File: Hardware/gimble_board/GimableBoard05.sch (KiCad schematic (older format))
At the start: 38 parts, among them Q1 Q_NMOS_GDS, Q2 Q_NMOS_GDS, Q3 Q_NMOS_GDS, Q4 Q_NMOS_GDS, Q5 Q_NMOS_GDS, Q6 Q_NMOS_GDS, Q7 Q_NMOS_GDS, Q8 Q_NMOS_GDS

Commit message: Fixed MOSFET's
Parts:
- removed D20, D21, D22, D23, D24, D25, D26: LED, symbol Device:LED
- removed Q2, Q3, Q4, Q5, Q6, Q7, Q8: Q_NMOS_GDS, symbol Device:Q_NMOS_GDS
- removed R26, R27, R28, R29, R30, R31, R32: 330, symbol Device:R
- removed R34, R35, R36, R37, R38, R39, R40: 500, symbol Device:R
- added D? (x7): LED, symbol Device:LED
- added Q? (x7): Q_NMOS_GDS, symbol Device:Q_NMOS_GDS
- added R? (x7): 330, symbol Device:R
- added R? (x7): 500, symbol Device:R
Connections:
- net +3V3: now also R25.1, R?.1, R?.1, R?.1, R?.1, R?.1, R?.1, R?.1; no longer R25.2
- net GND: now also Q1.3 (S), Q?.3 (S), Q?.3 (S), Q?.3 (S), Q?.3 (S), Q?.3 (S), Q?.3 (S), Q?.3 (S); no longer Q1.2 (D)
- net Servo_1_PWM: now also R33.1, R?.1, R?.1, R?.1, R?.1, R?.1, R?.1, R?.1; no longer R33.2
- net at D19.2 (A): now also R25.2; no longer R25.1
- net at D19.1 (K): now also Q1.2 (D); no longer Q1.3 (S)
- net at Q1.1 (G): now also R33.2; no longer R33.1
- new net: D?.2 (A), R?.2 (x7)
- new net: D?.1 (K), Q?.2 (D) (x7)
- new net: Q?.1 (G), R?.2 (x7)
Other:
- moved on the sheet: D19, Q1, R25, R33

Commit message: Annotated Symbols
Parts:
- gave numbers to parts that had none: 28
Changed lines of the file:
@@
 Servo_1_PWM
 $Comp
-L Device:R R?
+L Device:R R34
 U 1 1 5F8988CD
 P 3750 2100
-F 0 "R?" V 3650 2100 50  0000 C CNN
+F 0 "R34" V 3650 2100 50  0000 C CNN
 F 1 "330" V 3750 2100 50  0000 C CNN
 F 2 "" V 3680 2100 50  0001 C CNN
@@
 $EndComp
 $Comp
-L Device:LED D?
+L Device:LED D20
 U 1 1 5F8988D3
 P 3300 2100
-F 0 "D?" H 3300 2000 50  0000 C CNN
+F 0 "D20" H 3300 2000 50  0000 C CNN
 F 1 "LED" H 3300 2200 50  0000 C CNN
 F 2 "" H 3300 2100 50  0001 C CNN
@@
 $EndComp
 $Comp
-L Device:Q_NMOS_GDS Q?
+L Device:Q_NMOS_GDS Q2
 U 1 1 5F8988D9
 P 2800 2000
-F 0 "Q?" V 2800 2150 50  0000 C CNN
+F 0 "Q2" V 2800 2150 50  0000 C CNN
 F 1 "Q_NMOS_GDS" V 3050 2050 50  0000 C CNN
 F 2 "" H 3000 2100 50  0001 C CNN
@@
 $EndComp
 $Comp
-L Device:R R?
+L Device:R R26
 U 1 1 5F8988DF
 P 3100 1800
-F 0 "R?" V 3000 1800 50  0000 C CNN
+F 0 "R26" V 3000 1800 50  0000 C CNN
 F 1 "500" V 3100 1800 50  0000 C CNN
 F 2 "" V 3030 1800 50  0001 C CNN
@@
 Servo_1_PWM
 $Comp
-L Device:R R?
+L Device:R R35
 U 1 1 5F8A6B43
 P 3750 2750
-F 0 "R?" V 3650 2750 50  0000 C CNN
+F 0 "R35" V 3650 2750 50  0000 C CNN
 F 1 "330" V 3750 2750 50  0000 C CNN
 F 2 "" V 3680 2750 50  0001 C CNN
@@
 $EndComp
 $Comp
-L Device:LED D?
+L Device:LED D21
 U 1 1 5F8A6B49
 P 3300 2750
-F 0 "D?" H 3300 2650 50  0000 C CNN
+F 0 "D21" H 3300 2650 50  0000 C CNN
 F 1 "LED" H 3300 2850 50  0000 C CNN
 F 2 "" H 3300 2750 50  0001 C CNN
@@
 $EndComp
 $Comp
-L Device:Q_NMOS_GDS Q?
+L Device:Q_NMOS_GDS Q3
 U 1 1 5F8A6B4F
 P 2800 2650
-F 0 "Q?" V 2800 2800 50  0000 C CNN
+F 0 "Q3" V 2800 2800 50  0000 C CNN
 F 1 "Q_NMOS_GDS" V 3050 2700 50  0000 C CNN
 F 2 "" H 3000 2750 50  0001 C CNN
@@
 $EndComp
 $Comp
-L Device:R R?
+L Device:R R27
 U 1 1 5F8A6B55
 P 3100 2450
-F 0 "R?" V 3000 2450 50  0000 C CNN
+F 0 "R27" V 3000 2450 50  0000 C CNN
 F 1 "500" V 3100 2450 50  0000 C CNN
 F 2 "" V 3030 2450 50  0001 C CNN
@@
 Servo_1_PWM
 $Comp
-L Device:R R?
+L Device:R R36
 U 1 1 5F8A6B62
 P 3750 3400
-F 0 "R?" V 3650 3400 50  0000 C CNN
+F 0 "R36" V 3650 3400 50  0000 C CNN
 F 1 "330" V 3750 3400 50  0000 C CNN
 F 2 "" V 3680 3400 50  0001 C CNN
@@
 $EndComp
 $Comp
-L Device:LED D?
+L Device:LED D22
 U 1 1 5F8A6B68
 P 3300 3400
-F 0 "D?" H 3300 3300 50  0000 C CNN
+F 0 "D22" H 3300 3300 50  0000 C CNN
 F 1 "LED" H 3300 3500 50  0000 C CNN
 F 2 "" H 3300 3400 50  0001 C CNN
@@
 $EndComp
 $Comp
-L Device:Q_NMOS_GDS Q?
+L Device:Q_NMOS_GDS Q4
 U 1 1 5F8A6B6E
 P 2800 3300
-F 0 "Q?" V 2800 3450 50  0000 C CNN
+F 0 "Q4" V 2800 3450 50  0000 C CNN
 F 1 "Q_NMOS_GDS" V 3050 3350 50  0000 C CNN
 F 2 "" H 3000 3400 50  0001 C CNN
@@
 $EndComp
 $Comp
-L Device:R R?
+L Device:R R28
 U 1 1 5F8A6B74
 P 3100 3100
-F 0 "R?" V 3000 3100 50  0000 C CNN
+F 0 "R28" V 3000 3100 50  0000 C CNN
 F 1 "500" V 3100 3100 50  0000 C CNN
 F 2 "" V 3030 3100 50  0001 C CNN
@@
 Servo_1_PWM
 $Comp
-L Device:R R?
+L Device:R R37
 U 1 1 5F8C6A5B
 P 3750 4050
-F 0 "R?" V 3650 4050 50  0000 C CNN
+F 0 "R37" V 3650 4050 50  0000 C CNN
 F 1 "330" V 3750 4050 50  0000 C CNN
 F 2 "" V 3680 4050 50  0001 C CNN
@@
 $EndComp
 $Comp
-L Device:LED D?
+L Device:LED D23
 U 1 1 5F8C6A61
 P 3300 4050
-F 0 "D?" H 3300 3950 50  0000 C CNN
+F 0 "D23" H 3300 3950 50  0000 C CNN
 F 1 "LED" H 3300 4150 50  0000 C CNN
 F 2 "" H 3300 4050 50  0001 C CNN
@@
 $EndComp
 $Comp
-L Device:Q_NMOS_GDS Q?
+L Device:Q_NMOS_GDS Q5
 U 1 1 5F8C6A67
 P 2800 3950
-F 0 "Q?" V 2800 4100 50  0000 C CNN
+F 0 "Q5" V 2800 4100 50  0000 C CNN
 F 1 "Q_NMOS_GDS" V 3050 4000 50  0000 C CNN
 F 2 "" H 3000 4050 50  0001 C CNN
@@
 $EndComp
 $Comp
-L Device:R R?
+L Device:R R29
 U 1 1 5F8C6A6D
 P 3100 3750
-F 0 "R?" V 3000 3750 50  0000 C CNN
+F 0 "R29" V 3000 3750 50  0000 C CNN
 F 1 "500" V 3100 3750 50  0000 C CNN
 F 2 "" V 3030 3750 50  0001 C CNN
@@
 Servo_1_PWM
 $Comp
-L Device:R R?
+L Device:R R38
 U 1 1 5F8C6A7A
 P 3750 4700
-F 0 "R?" V 3650 4700 50  0000 C CNN
+F 0 "R38" V 3650 4700 50  0000 C CNN
 F 1 "330" V 3750 4700 50  0000 C CNN
 F 2 "" V 3680 4700 50  0001 C CNN
@@
 $EndComp
 $Comp
-L Device:LED D?
+L Device:LED D24
 U 1 1 5F8C6A80
 P 3300 4700
-F 0 "D?" H 3300 4600 50  0000 C CNN
+F 0 "D24" H 3300 4600 50  0000 C CNN
 F 1 "LED" H 3300 4800 50  0000 C CNN
 F 2 "" H 3300 4700 50  0001 C CNN
@@
 $EndComp
 $Comp
-L Device:Q_NMOS_GDS Q?
+L Device:Q_NMOS_GDS Q6
 U 1 1 5F8C6A86
 P 2800 4600
-F 0 "Q?" V 2800 4750 50  0000 C CNN
+F 0 "Q6" V 2800 4750 50  0000 C CNN
 F 1 "Q_NMOS_GDS" V 3050 4650 50  0000 C CNN
 F 2 "" H 3000 4700 50  0001 C CNN
@@
 $EndComp
 $Comp
-L Device:R R?
+L Device:R R30
 U 1 1 5F8C6A8C
 P 3100 4400
-F 0 "R?" V 3000 4400 50  0000 C CNN
+F 0 "R30" V 3000 4400 50  0000 C CNN
 F 1 "500" V 3100 4400 50  0000 C CNN
 F 2 "" V 3030 4400 50  0001 C CNN
@@
 Servo_1_PWM
 $Comp
-L Device:R R?
+L Device:R R39
 U 1 1 5F8C6A99
 P 3750 5350
-F 0 "R?" V 3650 5350 50  0000 C CNN
+F 0 "R39" V 3650 5350 50  0000 C CNN
 F 1 "330" V 3750 5350 50  0000 C CNN
 F 2 "" V 3680 5350 50  0001 C CNN
@@
 $EndComp
 $Comp
-L Device:LED D?
+L Device:LED D25
 U 1 1 5F8C6A9F
 P 3300 5350
-F 0 "D?" H 3300 5250 50  0000 C CNN
+F 0 "D25" H 3300 5250 50  0000 C CNN
 F 1 "LED" H 3300 5450 50  0000 C CNN
 F 2 "" H 3300 5350 50  0001 C CNN
@@
 $EndComp
 $Comp
-L Device:Q_NMOS_GDS Q?
+L Device:Q_NMOS_GDS Q7
 U 1 1 5F8C6AA5
 P 2800 5250
-F 0 "Q?" V 2800 5400 50  0000 C CNN
+F 0 "Q7" V 2800 5400 50  0000 C CNN
 F 1 "Q_NMOS_GDS" V 3050 5300 50  0000 C CNN
 F 2 "" H 3000 5350 50  0001 C CNN
@@
 $EndComp
 $Comp
-L Device:R R?
+L Device:R R31
 U 1 1 5F8C6AAB
 P 3100 5050
-F 0 "R?" V 3000 5050 50  0000 C CNN
+F 0 "R31" V 3000 5050 50  0000 C CNN
 F 1 "500" V 3100 5050 50  0000 C CNN
 F 2 "" V 3030 5050 50  0001 C CNN
@@
 Servo_1_PWM
 $Comp
-L Device:R R?
+L Device:R R40
 U 1 1 5F8C6AB8
 P 3750 6000
-F 0 "R?" V 3650 6000 50  0000 C CNN
+F 0 "R40" V 3650 6000 50  0000 C CNN
 F 1 "330" V 3750 6000 50  0000 C CNN
 F 2 "" V 3680 6000 50  0001 C CNN
@@
 $EndComp
 $Comp
-L Device:LED D?
+L Device:LED D26
 U 1 1 5F8C6ABE
 P 3300 6000
-F 0 "D?" H 3300 5900 50  0000 C CNN
+F 0 "D26" H 3300 5900 50  0000 C CNN
 F 1 "LED" H 3300 6100 50  0000 C CNN
 F 2 "" H 3300 6000 50  0001 C CNN
@@
 $EndComp
 $Comp
-L Device:Q_NMOS_GDS Q?
+L Device:Q_NMOS_GDS Q8
 U 1 1 5F8C6AC4
 P 2800 5900
-F 0 "Q?" V 2800 6050 50  0000 C CNN
+F 0 "Q8" V 2800 6050 50  0000 C CNN
 F 1 "Q_NMOS_GDS" V 3050 5950 50  0000 C CNN
 F 2 "" H 3000 6000 50  0001 C CNN
@@
 $EndComp
 $Comp
-L Device:R R?
+L Device:R R32
 U 1 1 5F8C6ACA
 P 3100 5700
-F 0 "R?" V 3000 5700 50  0000 C CNN
+F 0 "R32" V 3000 5700 50  0000 C CNN
 F 1 "500" V 3100 5700 50  0000 C CNN
 F 2 "" V 3030 5700 50  0001 C CNN

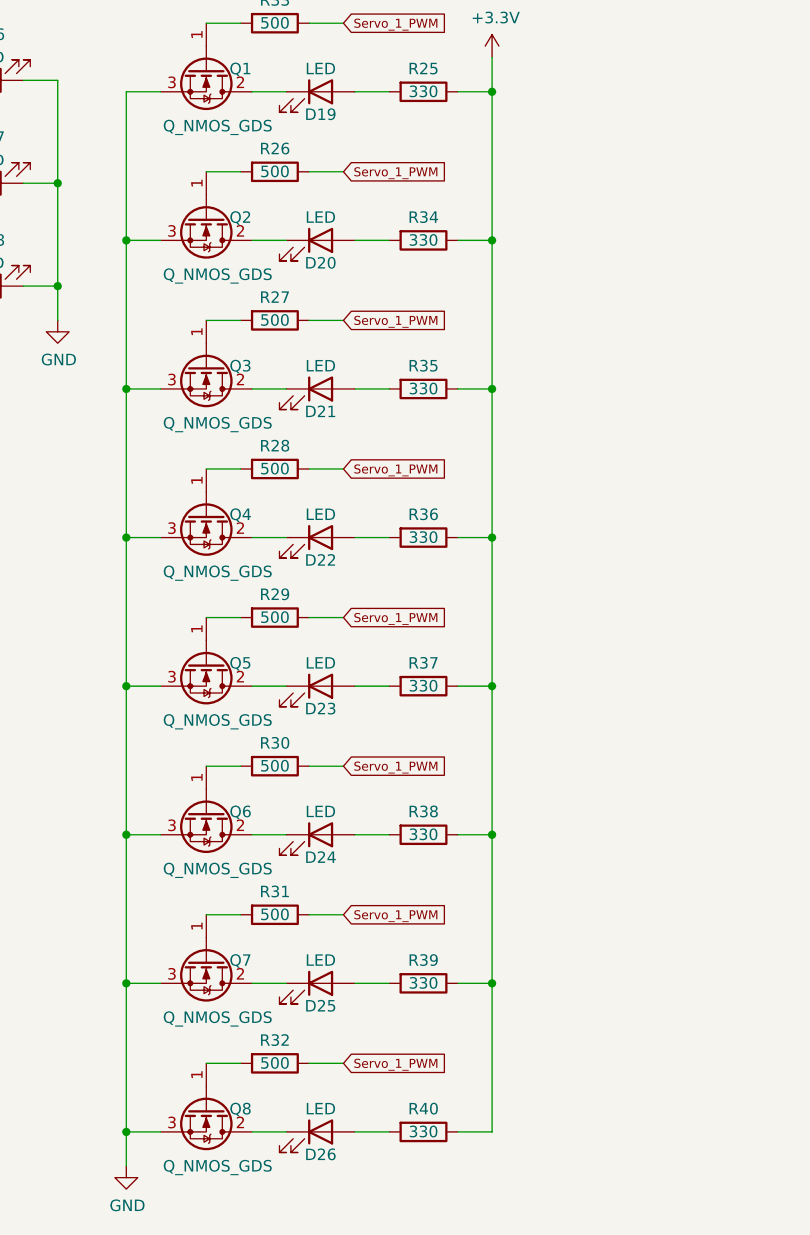
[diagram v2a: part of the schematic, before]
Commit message: Fixed Switch and Buttons
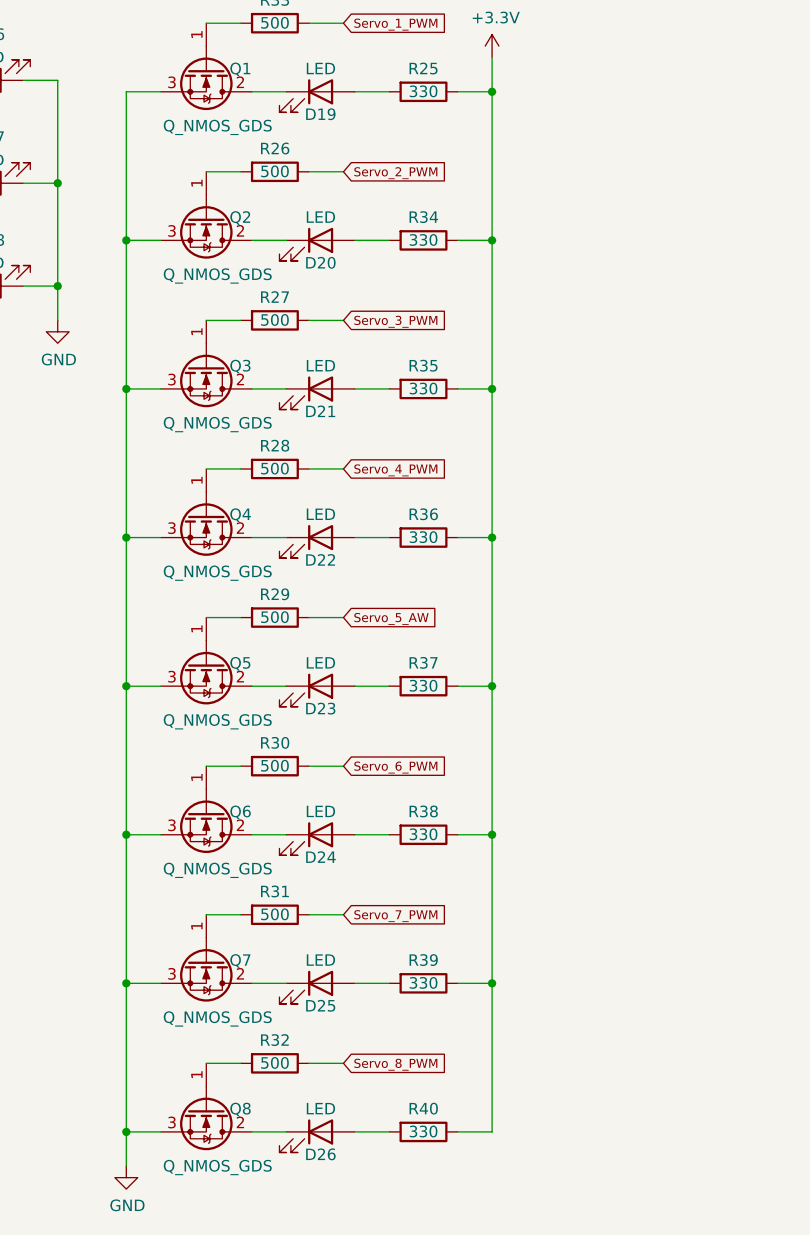
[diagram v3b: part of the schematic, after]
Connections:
- net Servo_1_PWM: no longer R26.1, R27.1, R28.1, R29.1, R30.1, R31.1, R32.1
- new net Servo_2_PWM: R26.1
- new net Servo_3_PWM: R27.1
- new net Servo_4_PWM: R28.1
- new net Servo_5_AW: R29.1
- new net Servo_6_PWM: R30.1
- new net Servo_7_PWM: R31.1
- new net Servo_8_PWM: R32.1
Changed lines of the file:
@@
 	3900 1450 4050 1450
 Text GLabel 3400 1800 2    39   Input ~ 0
-Servo_1_PWM
+Servo_2_PWM
 $Comp
 L Device:R R34
@@
 	3900 2100 4050 2100
 Text GLabel 3400 2450 2    39   Input ~ 0
-Servo_1_PWM
+Servo_3_PWM
 $Comp
 L Device:R R35
@@
 	3900 2750 4050 2750
 Text GLabel 3400 3100 2    39   Input ~ 0
-Servo_1_PWM
+Servo_4_PWM
 $Comp
 L Device:R R36
@@
 	3900 3400 4050 3400
 Text GLabel 3400 3750 2    39   Input ~ 0
-Servo_1_PWM
+Servo_5_AW
 $Comp
 L Device:R R37
@@
 	3900 4050 4050 4050
 Text GLabel 3400 4400 2    39   Input ~ 0
-Servo_1_PWM
+Servo_6_PWM
 $Comp
 L Device:R R38
@@
 	3900 4700 4050 4700
 Text GLabel 3400 5050 2    39   Input ~ 0
-Servo_1_PWM
+Servo_7_PWM
 $Comp
 L Device:R R39
@@
 	3900 5350 4050 5350
 Text GLabel 3400 5700 2    39   Input ~ 0
-Servo_1_PWM
+Servo_8_PWM
 $Comp
 L Device:R R40

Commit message: footprints
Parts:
- D19: renamed from D16; footprint (none) -> LED_SMD:LED_0603_1608Metric_Pad1.05x0.95mm_HandSolder
- D20: renamed from D17; footprint (none) -> LED_SMD:LED_0603_1608Metric_Pad1.05x0.95mm_HandSolder
- D21: renamed from D18; footprint (none) -> LED_SMD:LED_0603_1608Metric_Pad1.05x0.95mm_HandSolder
- D22: renamed from D19; footprint (none) -> LED_SMD:LED_0603_1608Metric_Pad1.05x0.95mm_HandSolder
- D23: renamed from D20; footprint (none) -> LED_SMD:LED_0603_1608Metric_Pad1.05x0.95mm_HandSolder
- D24: renamed from D21; footprint (none) -> LED_SMD:LED_0603_1608Metric_Pad1.05x0.95mm_HandSolder
- D25: renamed from D22; footprint (none) -> LED_SMD:LED_0603_1608Metric_Pad1.05x0.95mm_HandSolder
- D26: renamed from D23; footprint (none) -> LED_SMD:LED_0603_1608Metric_Pad1.05x0.95mm_HandSolder
- D27: renamed from D24; footprint (none) -> LED_SMD:LED_0603_1608Metric_Pad1.05x0.95mm_HandSolder
- D28: renamed from D25; footprint (none) -> LED_SMD:LED_0603_1608Metric_Pad1.05x0.95mm_HandSolder
- D29: renamed from D26; footprint (none) -> LED_SMD:LED_0603_1608Metric_Pad1.05x0.95mm_HandSolder
- Q1, Q2, Q3, Q4, Q5, Q6, Q7, Q8: footprint (none) -> Package_TO_SOT_SMD:SOT-23_Handsoldering
- R15: renamed from R22; footprint (none) -> Resistor_SMD:R_0603_1608Metric_Pad1.05x0.95mm_HandSolder
- R16: renamed from R23; footprint (none) -> Resistor_SMD:R_0603_1608Metric_Pad1.05x0.95mm_HandSolder
- R17: renamed from R24; footprint (none) -> Resistor_SMD:R_0603_1608Metric_Pad1.05x0.95mm_HandSolder
- R18: renamed from R33; footprint (none) -> Resistor_SMD:R_0603_1608Metric_Pad1.05x0.95mm_HandSolder
- R19: renamed from R26; footprint (none) -> Resistor_SMD:R_0603_1608Metric_Pad1.05x0.95mm_HandSolder
- R20: renamed from R27; footprint (none) -> Resistor_SMD:R_0603_1608Metric_Pad1.05x0.95mm_HandSolder
- R21: renamed from R28; footprint (none) -> Resistor_SMD:R_0603_1608Metric_Pad1.05x0.95mm_HandSolder
- R22: renamed from R29; footprint (none) -> Resistor_SMD:R_0603_1608Metric_Pad1.05x0.95mm_HandSolder
- R23: renamed from R30; footprint (none) -> Resistor_SMD:R_0603_1608Metric_Pad1.05x0.95mm_HandSolder
- R24: renamed from R31; footprint (none) -> Resistor_SMD:R_0603_1608Metric_Pad1.05x0.95mm_HandSolder
- R25: renamed from R32; footprint (none) -> Resistor_SMD:R_0603_1608Metric_Pad1.05x0.95mm_HandSolder
- R26: renamed from R25; footprint (none) -> Resistor_SMD:R_0603_1608Metric_Pad1.05x0.95mm_HandSolder
- R27: renamed from R34; footprint (none) -> Resistor_SMD:R_0603_1608Metric_Pad1.05x0.95mm_HandSolder
- R28: renamed from R35; footprint (none) -> Resistor_SMD:R_0603_1608Metric_Pad1.05x0.95mm_HandSolder
- R29: renamed from R36; footprint (none) -> Resistor_SMD:R_0603_1608Metric_Pad1.05x0.95mm_HandSolder
- R30: renamed from R37; footprint (none) -> Resistor_SMD:R_0603_1608Metric_Pad1.05x0.95mm_HandSolder
- R31: renamed from R38; footprint (none) -> Resistor_SMD:R_0603_1608Metric_Pad1.05x0.95mm_HandSolder
- R32: renamed from R39; footprint (none) -> Resistor_SMD:R_0603_1608Metric_Pad1.05x0.95mm_HandSolder
- R33: renamed from R40; footprint (none) -> Resistor_SMD:R_0603_1608Metric_Pad1.05x0.95mm_HandSolder

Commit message: layout 2
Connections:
- net Servo_5_AW renamed Servo_5_PWM
- net Servo_8_PWM renamed Servo_8_AW
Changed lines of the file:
@@
 	3900 3400 4050 3400
 Text GLabel 3400 3750 2    39   Input ~ 0
-Servo_5_AW
+Servo_5_PWM
 $Comp
 L Device:R R30
@@
 	3900 5350 4050 5350
 Text GLabel 3400 5700 2    39   Input ~ 0
-Servo_8_PWM
+Servo_8_AW
 $Comp
 L Device:R R33

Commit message: layout 4
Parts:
- removed D19, D20, D21: LED, LED_SMD:LED_0603_1608Metric_Pad1.05x0.95mm_HandSolder, symbol Device:LED
- removed R15: 1k, Resistor_SMD:R_0603_1608Metric_Pad1.05x0.95mm_HandSolder, symbol Device:R
- removed R16: 500, Resistor_SMD:R_0603_1608Metric_Pad1.05x0.95mm_HandSolder, symbol Device:R
- removed R17: 330, Resistor_SMD:R_0603_1608Metric_Pad1.05x0.95mm_HandSolder, symbol Device:R
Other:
- note removed: "Power Indicators"
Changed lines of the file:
@@
 EESchema Schematic File Version 4
-LIBS:gimble_board-cache
 EELAYER 30 0
 EELAYER END
@@
 Comment4 ""
 $EndDescr
-$Comp
-L power:+12V #PWR034
-U 1 1 5FB4BC1F
-P 1100 1250
-F 0 "#PWR034" H 1100 1100 50  0001 C CNN
-F 1 "+12V" H 1115 1423 50  0000 C CNN
-F 2 "" H 1100 1250 50  0001 C CNN
-F 3 "" H 1100 1250 50  0001 C CNN
-	1    1100 1250
-	1    0    0    -1
-$EndComp
-$Comp
-L Device:R R15
-U 1 1 5FB4CC27
-P 1400 1400
-F 0 "R15" V 1300 1400 50  0000 C CNN
-F 1 "1k" V 1400 1400 50  0000 C CNN
-F 2 "Resistor_SMD:R_0603_1608Metric_Pad1.05x0.95mm_HandSolder" V 1330 1400 50  0001 C CNN
-F 3 "~" H 1400 1400 50  0001 C CNN
-	1    1400 1400
-	0    1    1    0
-$EndComp
-$Comp
-L Device:LED D19
-U 1 1 5FB4D7BE
-P 1850 1400
-F 0 "D19" H 1850 1200 50  0000 C CNN
-F 1 "LED" H 1850 1300 50  0000 C CNN
-F 2 "LED_SMD:LED_0603_1608Metric_Pad1.05x0.95mm_HandSolder" H 1850 1400 50  0001 C CNN
-F 3 "~" H 1850 1400 50  0001 C CNN
-	1    1850 1400
-	-1   0    0    1
-$EndComp
-Wire Wire Line
-	1100 1250 1100 1400
-Wire Wire Line
-	1100 1400 1250 1400
-Wire Wire Line
-	1550 1400 1700 1400
-$Comp
-L Device:R R16
-U 1 1 5FB50DC0
-P 1400 1850
-F 0 "R16" V 1300 1850 50  0000 C CNN
-F 1 "500" V 1400 1850 50  0000 C CNN
-F 2 "Resistor_SMD:R_0603_1608Metric_Pad1.05x0.95mm_HandSolder" V 1330 1850 50  0001 C CNN
-F 3 "~" H 1400 1850 50  0001 C CNN
-	1    1400 1850
-	0    1    1    0
-$EndComp
-$Comp
-L Device:LED D20
-U 1 1 5FB50DC6
-P 1850 1850
-F 0 "D20" H 1850 1650 50  0000 C CNN
-F 1 "LED" H 1850 1750 50  0000 C CNN
-F 2 "LED_SMD:LED_0603_1608Metric_Pad1.05x0.95mm_HandSolder" H 1850 1850 50  0001 C CNN
-F 3 "~" H 1850 1850 50  0001 C CNN
-	1    1850 1850
-	-1   0    0    1
-$EndComp
-Wire Wire Line
-	1100 1700 1100 1850
-Wire Wire Line
-	1100 1850 1250 1850
-Wire Wire Line
-	1550 1850 1700 1850
-$Comp
-L Device:R R17
-U 1 1 5FB519B8
-P 1400 2300
-F 0 "R17" V 1300 2300 50  0000 C CNN
-F 1 "330" V 1400 2300 50  0000 C CNN
-F 2 "Resistor_SMD:R_0603_1608Metric_Pad1.05x0.95mm_HandSolder" V 1330 2300 50  0001 C CNN
-F 3 "~" H 1400 2300 50  0001 C CNN
-	1    1400 2300
-	0    1    1    0
-$EndComp
-$Comp
-L Device:LED D21
-U 1 1 5FB519BE
-P 1850 2300
-F 0 "D21" H 1850 2100 50  0000 C CNN
-F 1 "LED" H 1850 2200 50  0000 C CNN
-F 2 "LED_SMD:LED_0603_1608Metric_Pad1.05x0.95mm_HandSolder" H 1850 2300 50  0001 C CNN
-F 3 "~" H 1850 2300 50  0001 C CNN
-	1    1850 2300
-	-1   0    0    1
-$EndComp
-Wire Wire Line
-	1100 2150 1100 2300
-Wire Wire Line
-	1100 2300 1250 2300
-Wire Wire Line
-	1550 2300 1700 2300
-$Comp
-L power:+3.3V #PWR036
-U 1 1 5FB51C08
-P 1100 2150
-F 0 "#PWR036" H 1100 2000 50  0001 C CNN
-F 1 "+3.3V" H 1115 2323 50  0000 C CNN
-F 2 "" H 1100 2150 50  0001 C CNN
-F 3 "" H 1100 2150 50  0001 C CNN
-	1    1100 2150
-	1    0    0    -1
-$EndComp
-$Comp
-L power:+5V #PWR035
-U 1 1 5FB523C2
-P 1100 1700
-F 0 "#PWR035" H 1100 1550 50  0001 C CNN
-F 1 "+5V" H 1115 1873 50  0000 C CNN
-F 2 "" H 1100 1700 50  0001 C CNN
-F 3 "" H 1100 1700 50  0001 C CNN
-	1    1100 1700
-	1    0    0    -1
-$EndComp
-$Comp
-L power:GND #PWR037
-U 1 1 5FB5276D
-P 2150 2450
-F 0 "#PWR037" H 2150 2200 50  0001 C CNN
-F 1 "GND" H 2155 2277 50  0000 C CNN
-F 2 "" H 2150 2450 50  0001 C CNN
-F 3 "" H 2150 2450 50  0001 C CNN
-	1    2150 2450
-	1    0    0    -1
-$EndComp
-Wire Wire Line
-	2000 1400 2150 1400
-Wire Wire Line
-	2150 1400 2150 1850
-Wire Wire Line
-	2000 2300 2150 2300
-Connection ~ 2150 2300
-Wire Wire Line
-	2150 2300 2150 2450
-Wire Wire Line
-	2000 1850 2150 1850
-Connection ~ 2150 1850
-Wire Wire Line
-	2150 1850 2150 2300
 $Comp
 L power:+3.3V #PWR039
@@
 	1    0    0    -1
 $EndComp
-Text Notes 1050 900  0    79   ~ 0
-Power Indicators
 Text Notes 2850 900  0    79   ~ 0
 Servo Indicators
